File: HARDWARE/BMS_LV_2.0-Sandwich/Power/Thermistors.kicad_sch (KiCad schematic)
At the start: 25 parts, among them J6 Conn_01x09_Female

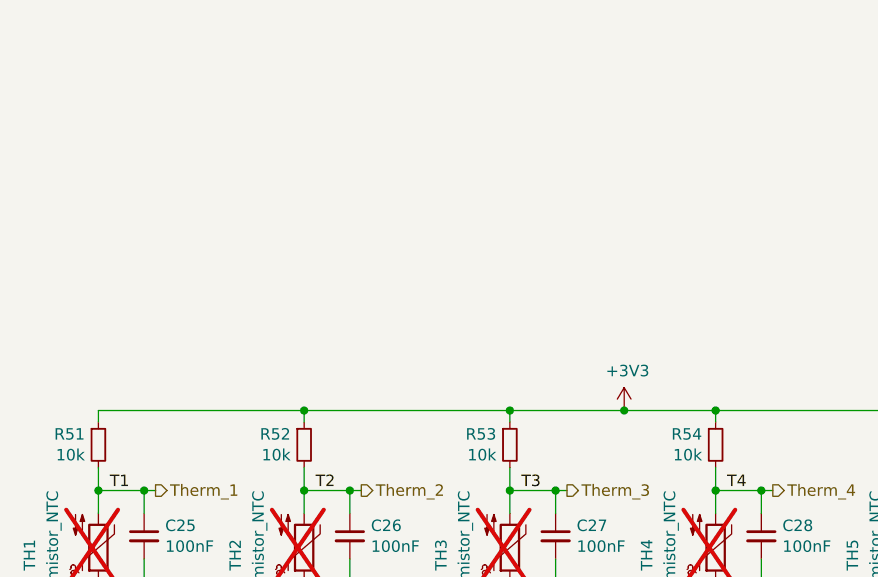
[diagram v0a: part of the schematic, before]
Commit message: Zmiany w power: nowe bezpieczniki, nowy wymienialny layout dla tych bezpiecznikow, dodano diode zenera dla stabilizacji napięcia, zmiany dla control:  wyjebany eeprom, przesunięty can, zmieniony layout przetwornic, dodano programator i tvs, jeszcze do dokonczenia routing w control.
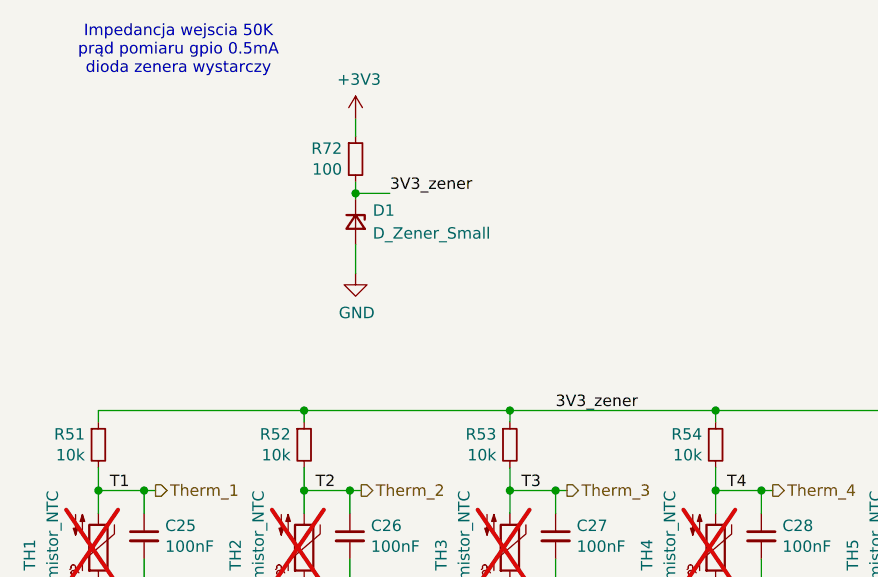
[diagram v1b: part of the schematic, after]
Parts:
- added D1: D_Zener_Small, Diode_SMD:D_0805_2012Metric_Pad1.15x1.40mm_HandSolder, symbol Device:D_Zener_Small
- added R72: 100, Resistor_SMD:R_0603_1608Metric, symbol Device:R_Small
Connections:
- net +3V3: now also R72.1; no longer R51.1, R52.1, R53.1, R54.1, R55.1, R56.1, R63.1, R64.1
- net GND: now also D1.2 (A)
- new net 3V3_zener: D1.1 (K), R51.1, R52.1, R53.1, R54.1, R55.1, R56.1, R63.1, R64.1, R72.2
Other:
- note added: "Impedancja wejscia 50K prąd pomiaru gpio 0.5mA dioda zenera wystarczy"
